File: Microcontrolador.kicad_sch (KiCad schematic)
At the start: 2 parts

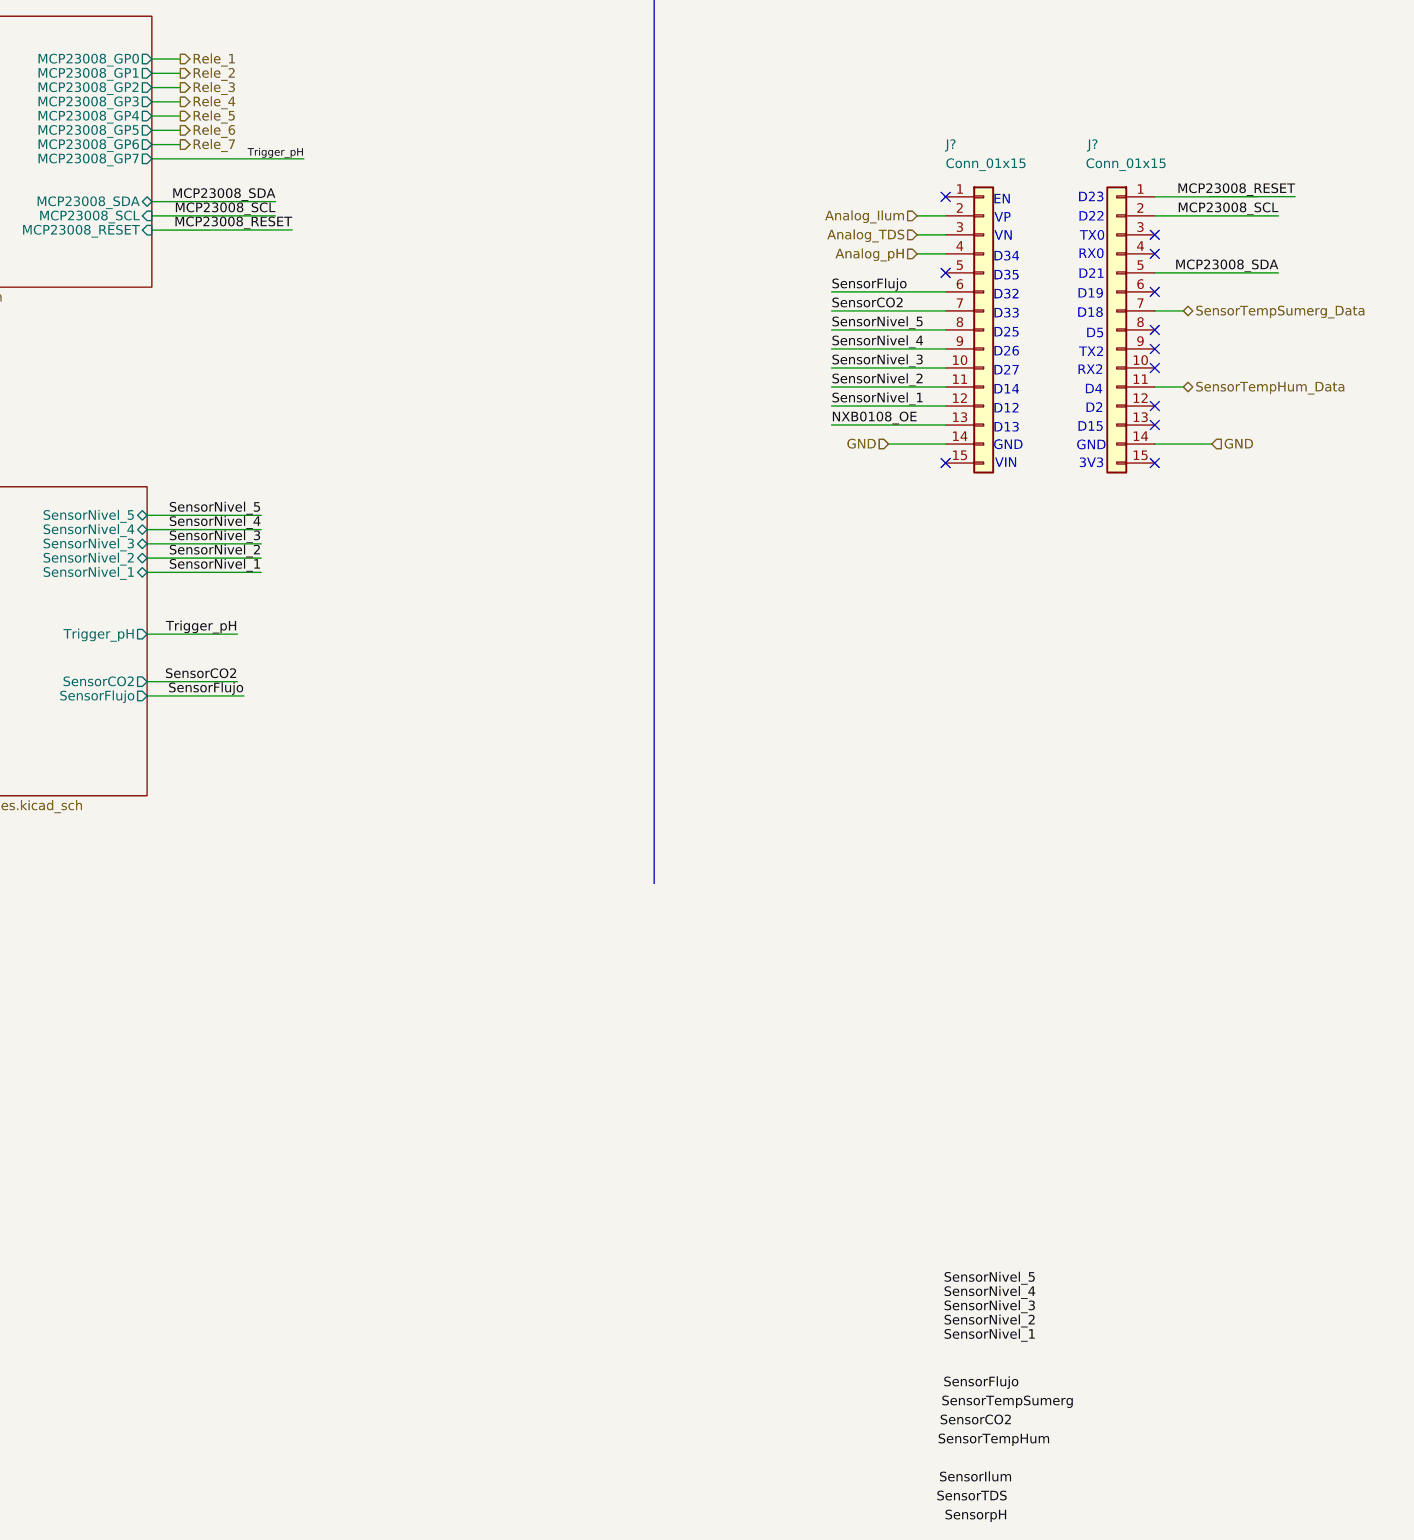
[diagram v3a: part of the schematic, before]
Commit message: Actualización de SCH según placa industrial, y búsqueda de footprints.
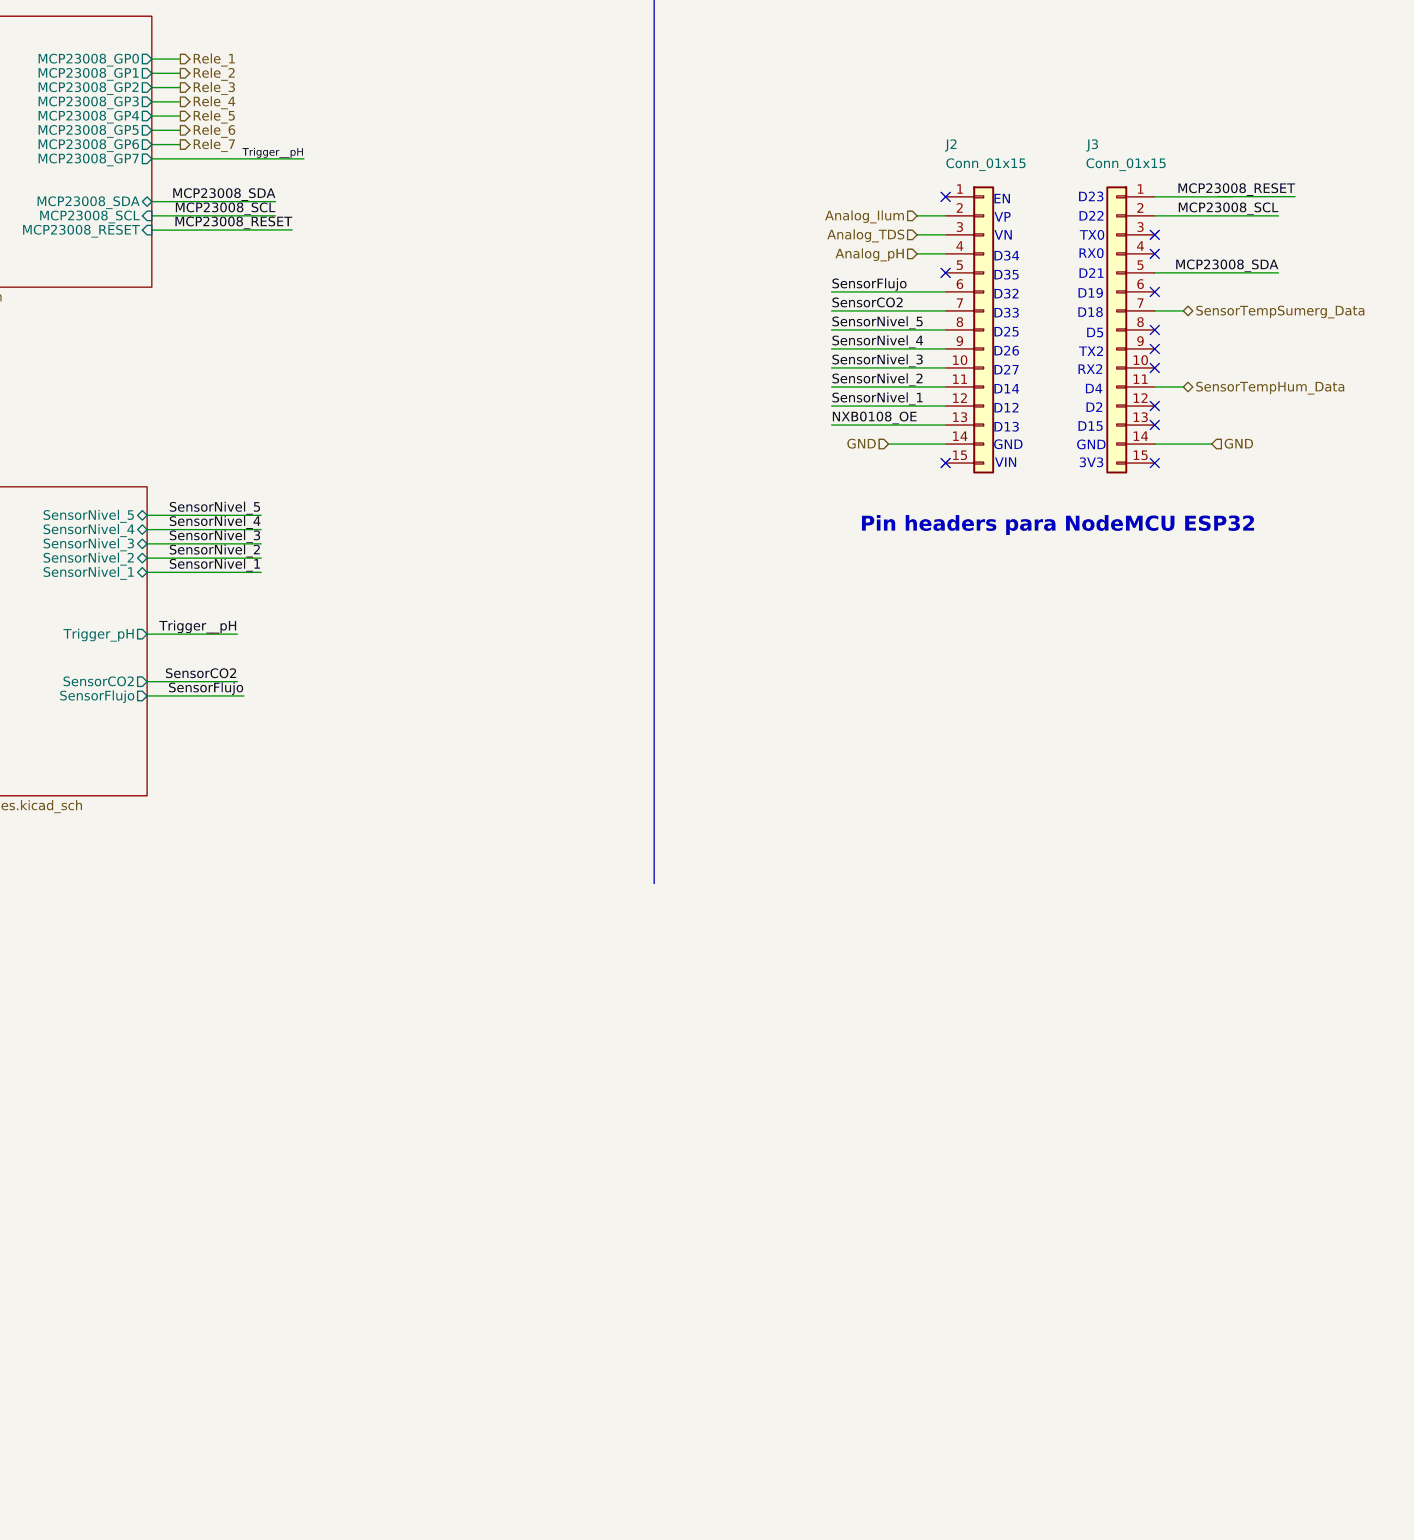
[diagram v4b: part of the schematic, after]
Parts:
- gave numbers to parts that had none: 2
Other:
- note added: "Pin headers para NodeMCU ESP32"
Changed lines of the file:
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@@
     (effects (font (size 1.27 1.27)) (justify left bottom))
+  )
+  (text "Pin headers para NodeMCU ESP32" (at 204.47 119.38 0)
+    (effects (font (size 2 2) (thickness 0.254) bold) (justify left bottom))
   )
   (label "MCP23008_RESET" (at 128.6002 78.7146 180)
@@
     (effects (font (size 1.27 1.27)) (justify left bottom))
   )
-  (label "SensorNivel_2" (at 227.965 225.425 180)
-    (effects (font (size 1.27 1.27)) (justify right bottom))
-  )
   (label "MCP23008_SCL" (at 126.365 76.835 180)
-    (effects (font (size 1.27 1.27)) (justify right bottom))
-  )
-  (label "SensorTDS" (at 224.155 248.92 180)
     (effects (font (size 1.27 1.27)) (justify right bottom))
   )
@@
     (effects (font (size 1.27 1.27)) (justify right bottom))
   )
-  (label "SensorNivel_4" (at 227.965 221.615 180)
-    (effects (font (size 1.27 1.27)) (justify right bottom))
-  )
   (label "SensorNivel_2" (at 200.66 99.695 0)
     (effects (font (size 1.27 1.27)) (justify left bottom))
   )
-  (label "Trigger_pH" (at 121.285 132.715 180)
-    (effects (font (size 1.27 1.27)) (justify right bottom))
-  )
-  (label "SensorNivel_5" (at 227.965 219.71 180)
+  (label "Trigger__pH" (at 121.285 132.715 180)
     (effects (font (size 1.27 1.27)) (justify right bottom))
   )
   (label "SensorFlujo" (at 122.1486 140.97 180)
-    (effects (font (size 1.27 1.27)) (justify right bottom))
-  )
-  (label "SensorNivel_1" (at 227.965 227.33 180)
     (effects (font (size 1.27 1.27)) (justify right bottom))
   )
@@
     (effects (font (size 1.27 1.27)) (justify left bottom))
   )
-  (label "SensorpH" (at 224.155 251.46 180)
-    (effects (font (size 1.27 1.27)) (justify right bottom))
-  )
   (label "NXB0108_OE" (at 200.66 104.775 0)
     (effects (font (size 1.27 1.27)) (justify left bottom))
   )
-  (label "Trigger_pH" (at 130.175 69.215 180)
+  (label "Trigger__pH" (at 130.175 69.215 180)
     (effects (font (size 1 1)) (justify right bottom))
   )
   (label "SensorNivel_3" (at 200.66 97.155 0)
     (effects (font (size 1.27 1.27)) (justify left bottom))
-  )
-  (label "SensorCO2" (at 224.79 238.76 180)
-    (effects (font (size 1.27 1.27)) (justify right bottom))
   )
   (label "MCP23008_RESET" (at 262.5852 74.2696 180)
@@
     (effects (font (size 1.27 1.27)) (justify right bottom))
   )
-  (label "SensorTempHum" (at 229.87 241.3 180)
-    (effects (font (size 1.27 1.27)) (justify right bottom))
-  )
   (label "MCP23008_SCL" (at 260.35 76.835 180)
-    (effects (font (size 1.27 1.27)) (justify right bottom))
-  )
-  (label "SensorTempSumerg" (at 233.045 236.22 180)
     (effects (font (size 1.27 1.27)) (justify right bottom))
   )
@@
     (effects (font (size 1.27 1.27)) (justify right bottom))
   )
-  (label "SensorNivel_3" (at 227.965 223.52 180)
-    (effects (font (size 1.27 1.27)) (justify right bottom))
-  )
   (label "SensorNivel_4" (at 124.46 118.745 180)
-    (effects (font (size 1.27 1.27)) (justify right bottom))
-  )
-  (label "SensorFlujo" (at 225.7044 233.68 180)
     (effects (font (size 1.27 1.27)) (justify right bottom))
   )
@@
   (label "SensorNivel_5" (at 200.66 92.075 0)
     (effects (font (size 1.27 1.27)) (justify left bottom))
-  )
-  (label "SensorIlum" (at 224.79 246.38 180)
-    (effects (font (size 1.27 1.27)) (justify right bottom))
   )
   (hierarchical_label "SensorTempHum_Data" (shape bidirectional) (at 247.65 99.695 0)
@@
   (symbol (lib_id "Connector_Generic:Conn_01x15") (at 238.76 92.075 0) (mirror y) (unit 1)
     (in_bom yes) (on_board yes)
-    (property "Reference" "J?" (id 0) (at 235.585 67.31 0))
+    (property "Reference" "J3" (id 0) (at 235.585 67.31 0))
     (property "Value" "Conn_01x15" (id 1) (at 240.03 69.85 0))
     (property "Footprint" "Connector_JST:JST_SUR_SM08B-SURS-TF_1x08-1MP_P0.80mm_Horizontal" (id 2) (at 238.76 92.075 0)
@@
   (symbol (lib_id "Connector_Generic:Conn_01x15") (at 220.98 92.075 0) (unit 1)
     (in_bom yes) (on_board yes)
-    (property "Reference" "J?" (id 0) (at 215.9 67.31 0)
+    (property "Reference" "J2" (id 0) (at 215.9 67.31 0)
       (effects (font (size 1.27 1.27)) (justify left))
     )

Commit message: Fin de SCH, config de inicio para PCB
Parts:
- J2, J3: footprint Connector_JST:JST_SUR_SM08B-SURS-TF_1x08-1MP_P0.80mm_Horizontal -> Connector_PinHeader_2.54mm:PinHeader_1x15_P2.54mm_Vertical
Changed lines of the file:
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@@
     (property "Reference" "J3" (id 0) (at 235.585 67.31 0))
     (property "Value" "Conn_01x15" (id 1) (at 240.03 69.85 0))
-    (property "Footprint" "Connector_JST:JST_SUR_SM08B-SURS-TF_1x08-1MP_P0.80mm_Horizontal" (id 2) (at 238.76 92.075 0)
+    (property "Footprint" "Connector_PinHeader_2.54mm:PinHeader_1x15_P2.54mm_Vertical" (id 2) (at 238.76 92.075 0)
       (effects (font (size 1.27 1.27)) hide)
     )
@@
       (effects (font (size 1.27 1.27)) (justify left))
     )
-    (property "Footprint" "Connector_JST:JST_SUR_SM08B-SURS-TF_1x08-1MP_P0.80mm_Horizontal" (id 2) (at 220.98 92.075 0)
+    (property "Footprint" "Connector_PinHeader_2.54mm:PinHeader_1x15_P2.54mm_Vertical" (id 2) (at 220.98 92.075 0)
       (effects (font (size 1.27 1.27)) hide)
     )
